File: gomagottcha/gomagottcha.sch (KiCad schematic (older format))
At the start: 77 parts

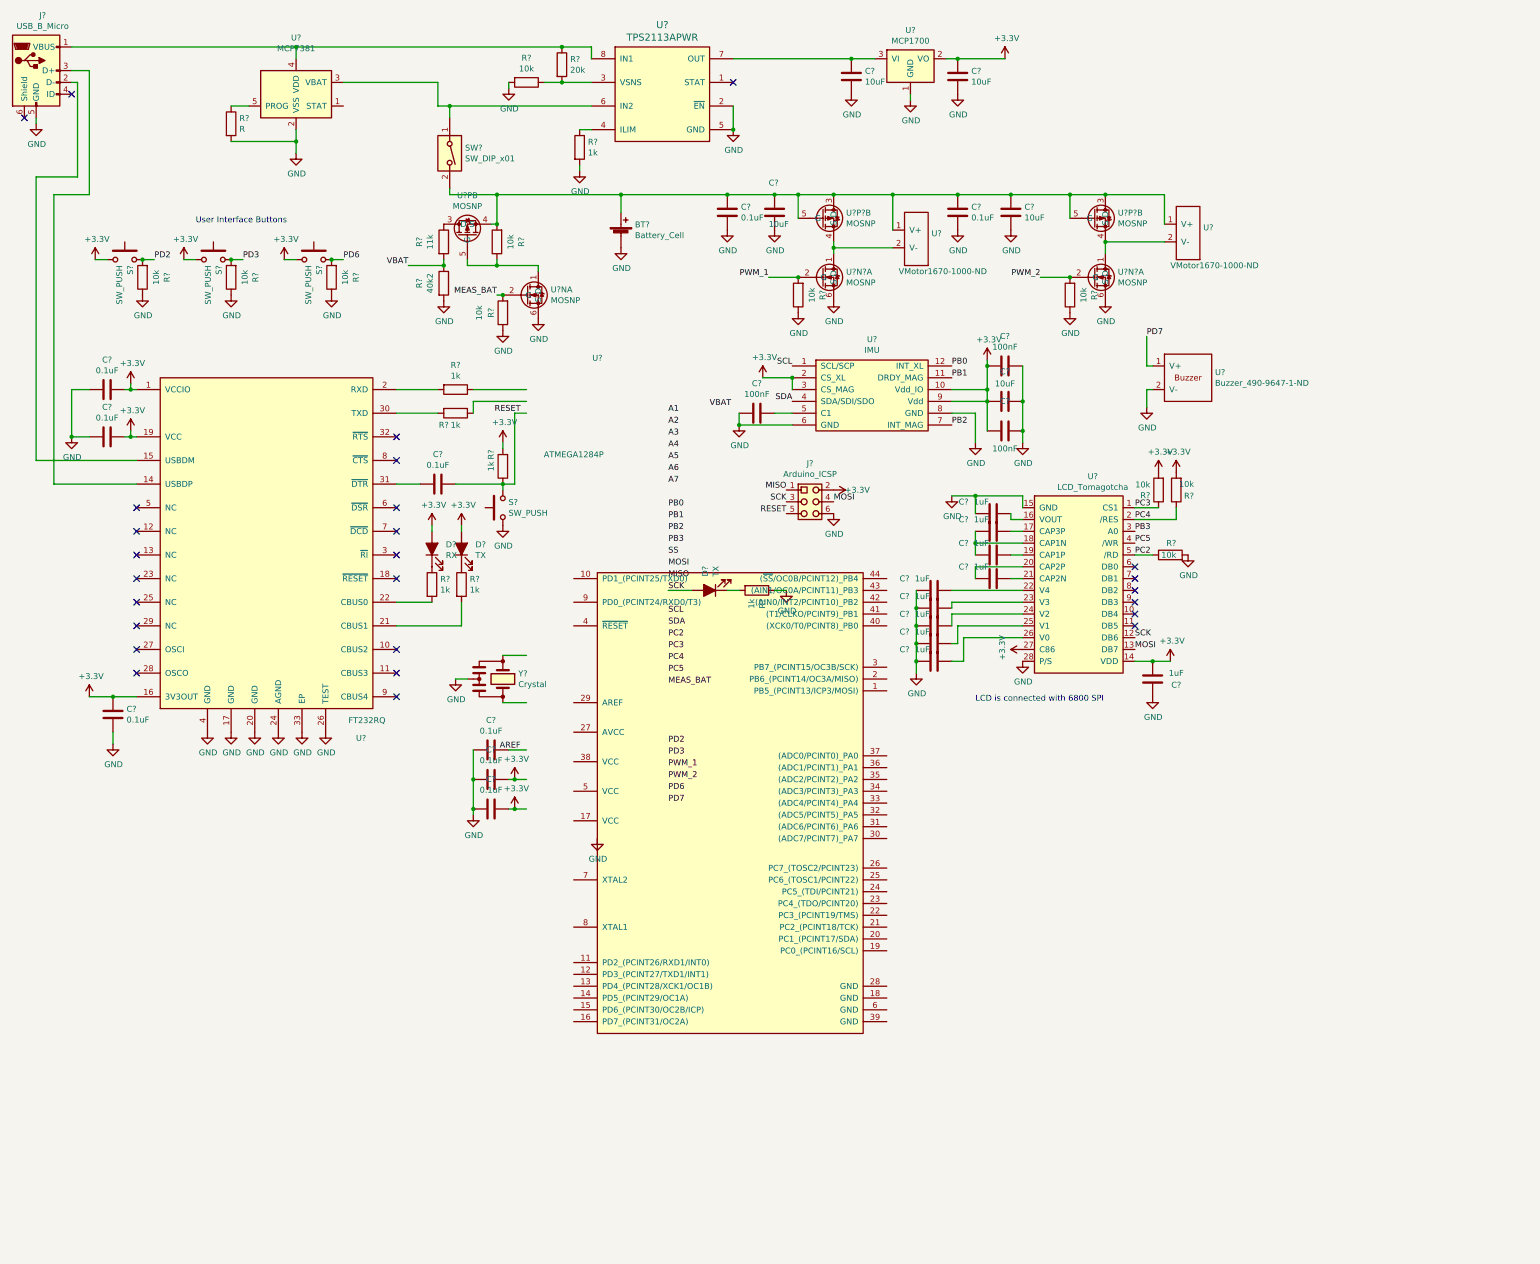
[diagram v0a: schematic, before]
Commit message: BLE hooked up
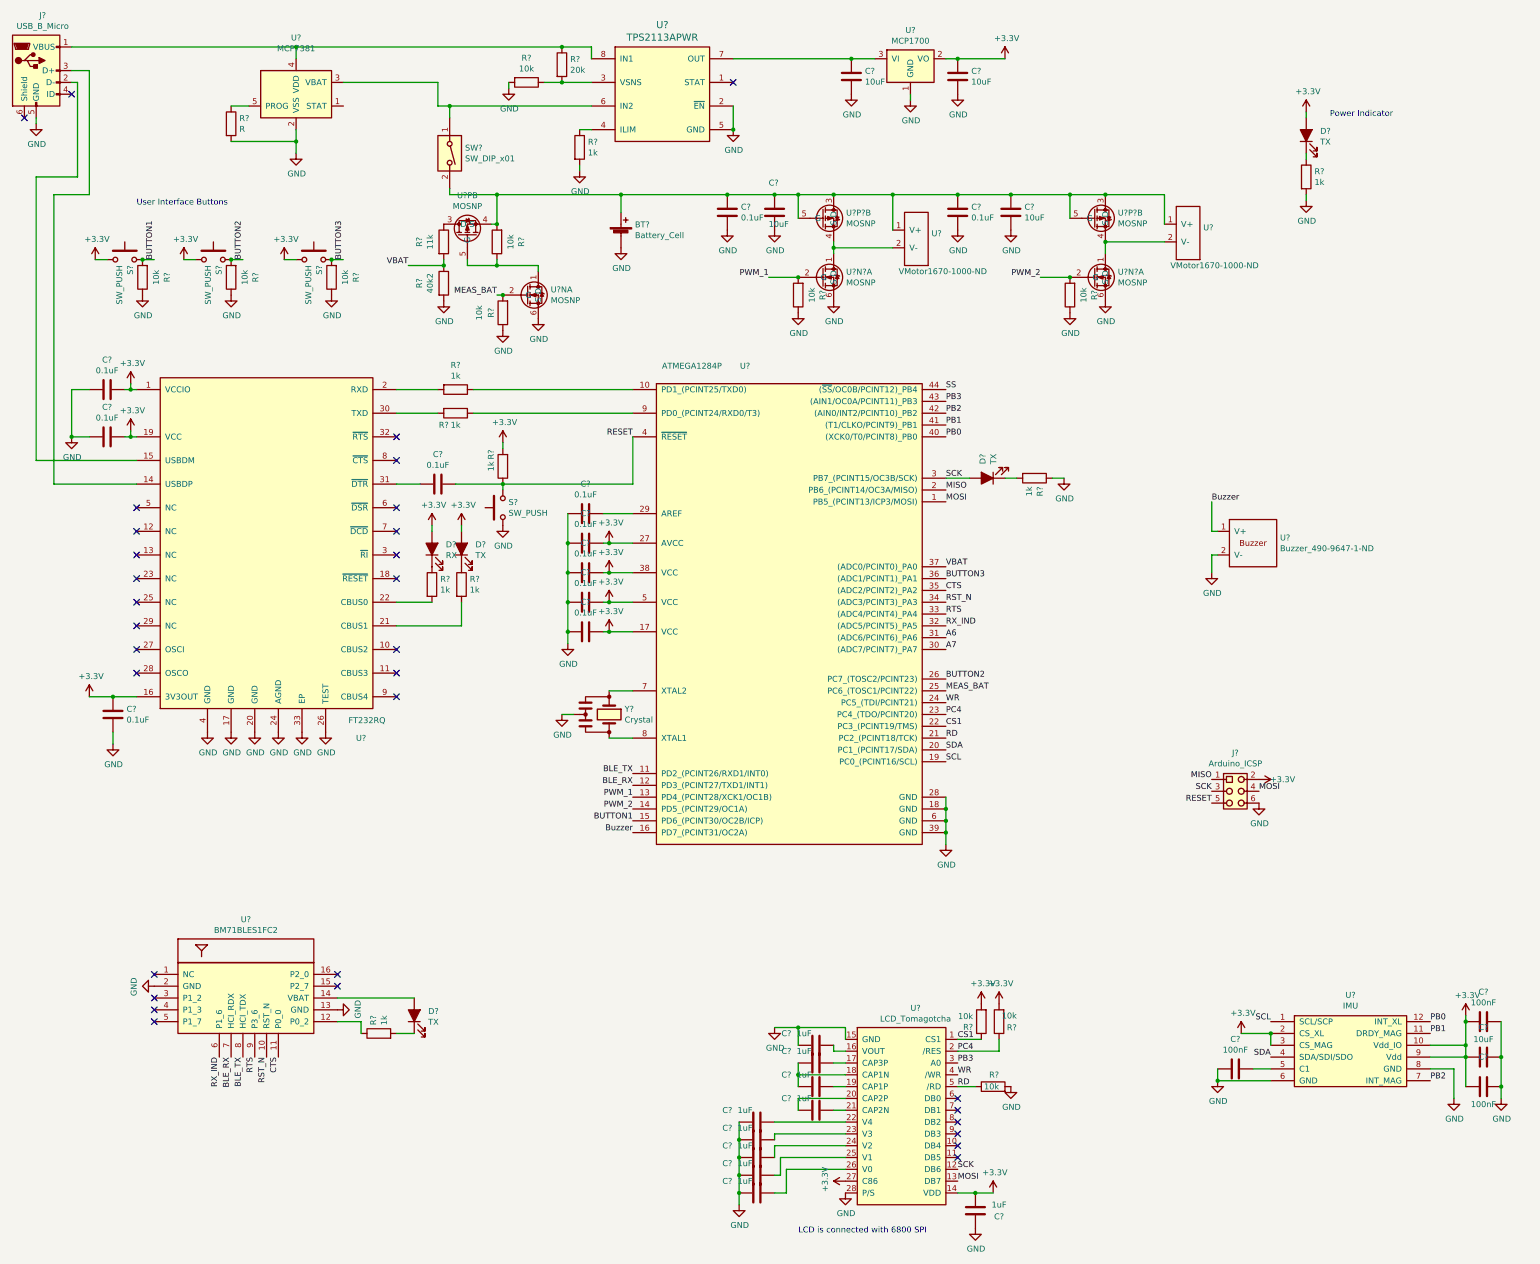
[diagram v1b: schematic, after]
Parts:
- added C? (x2): 0.1uF, symbol tama-sym:C
- added D? (x2): TX, symbol tama-sym:LED_ALT
- added R? (x2): 1k, symbol Device:R
- added U?: BM71BLES1FC2, symbol tama-sym:BM71BLES1FC2
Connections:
- net labels added: BLE_RX, BLE_TX, BUTTON1, BUTTON2, BUTTON3, Buzzer, CS1, CTS, RD, RST_N, RTS, RX_IND, WR
- net labels removed: A1, A2, A3, A4, A5, AREF, PC2, PC3, PC5, PD2, PD3, PD6, PD7
- wire segments 176 -> 191
- no-connect marks 26 -> 32
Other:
- note added: "Power Indicator"
- moved on the sheet: C?, D?, J?, R?, U?, Y?

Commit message: TO DO: Finish assigning footprints
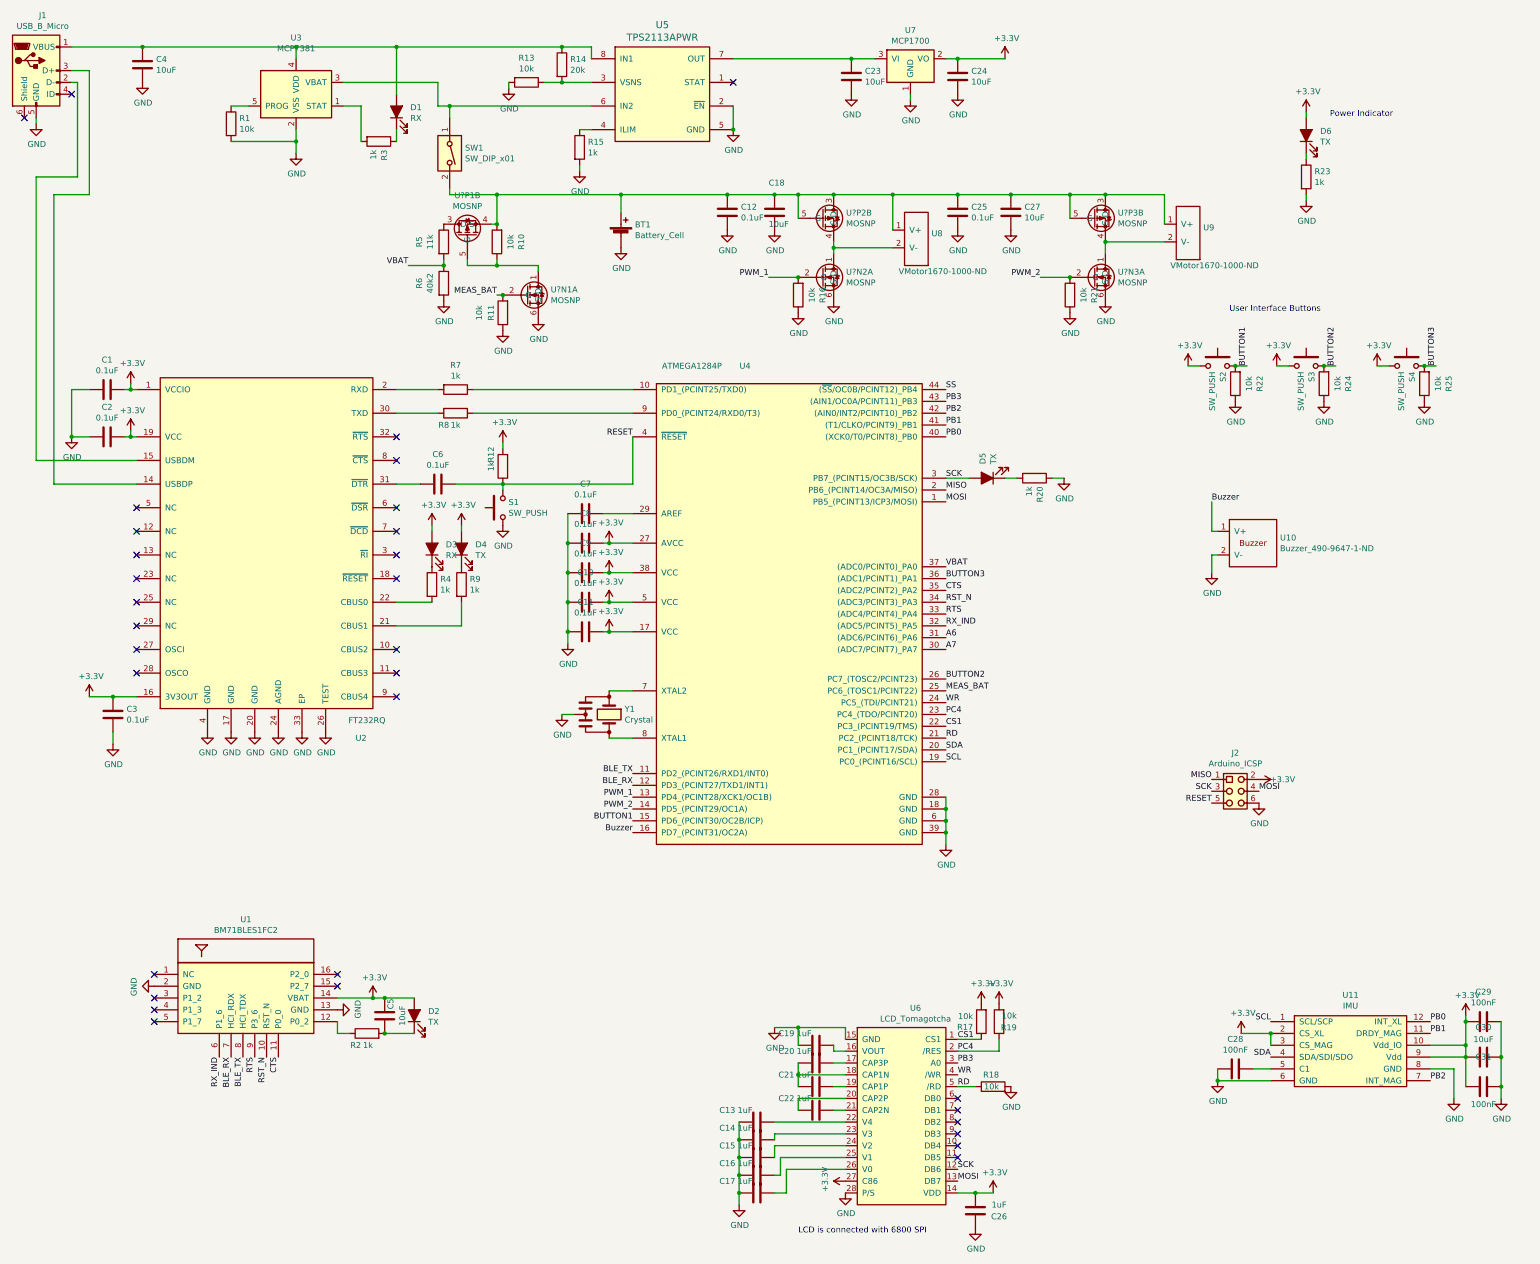
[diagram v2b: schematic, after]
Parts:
- added C4, C5: 10uF, tama-footprints:C_0603_1608Metric, symbol tama-sym:C
- added D1: RX, symbol tama-sym:LED_ALT
- added R3: 1k, tama-footprints:R_0603_1608Metric, symbol Device:R
- C1, C10, C11, C12, C13, C14, C15, C16, C17, C18, C19, C2, C20, C21, C22, C23, C24, C25, C26, C27, C28, C29, C3, C30, C31, C6, C7, C8, C9: renamed from C?; footprint (none) -> tama-footprints:C_0603_1608Metric
- R1: renamed from R?; value R -> 10k; footprint (none) -> tama-footprints:R_0603_1608Metric
- R10, R11, R12, R13, R14, R15, R16, R17, R18, R19, R2, R20, R21, R22, R23, R24, R25, R4, R5, R6, R7, R8, R9: renamed from R?; footprint (none) -> tama-footprints:R_0603_1608Metric
- S1, S2, S3, S4: renamed from S?; footprint (none) -> tama-footprints:Pushbutton_EG4791-ND
- SW1: renamed from SW?; footprint (none) -> tama-footprints:Switch_CWI333-ND
- U1: renamed from U?; footprint (none) -> tama-footprints:BM71BLE
- U2: renamed from U?; footprint Package_SO:TSSOP-28_4.4x9.7mm_P0.65mm -> tama-footprints:QFN-32-1EP_5x5mm_P0.5mm_EP3.1x3.1mm_ThermalVias
- U4: renamed from U?; footprint (none) -> tama-footprints:TQFP-44_10x10mm_P0.8mm
- U5: renamed from U?; footprint Package_SO:TSSOP-8_4.4x3mm_P0.65mm -> tama-footprints:VSON-8_3.1x3.1mm_P0.65mm
- gave numbers to parts that had none: 20
- renumbered U?N to U?N1, U?P to U?P1
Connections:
- net +3V3: now also D2.2 (A), U1.14 (VBAT), C5.1
- net GND: now also C4.2
- net at J1.1 (VBUS), R14.1, U3.4 (VDD)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: now also C4.1, D1.2 (A)
- net at U3.1 (STAT): now also R3.2
- net at D2.1 (K), R2.2: now also C5.2
- new net: D1.1 (K), R3.1
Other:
- moved on the sheet: R2, R22, R24, R25, S2, S3, S4

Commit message: TODO: replace FT232R symbol
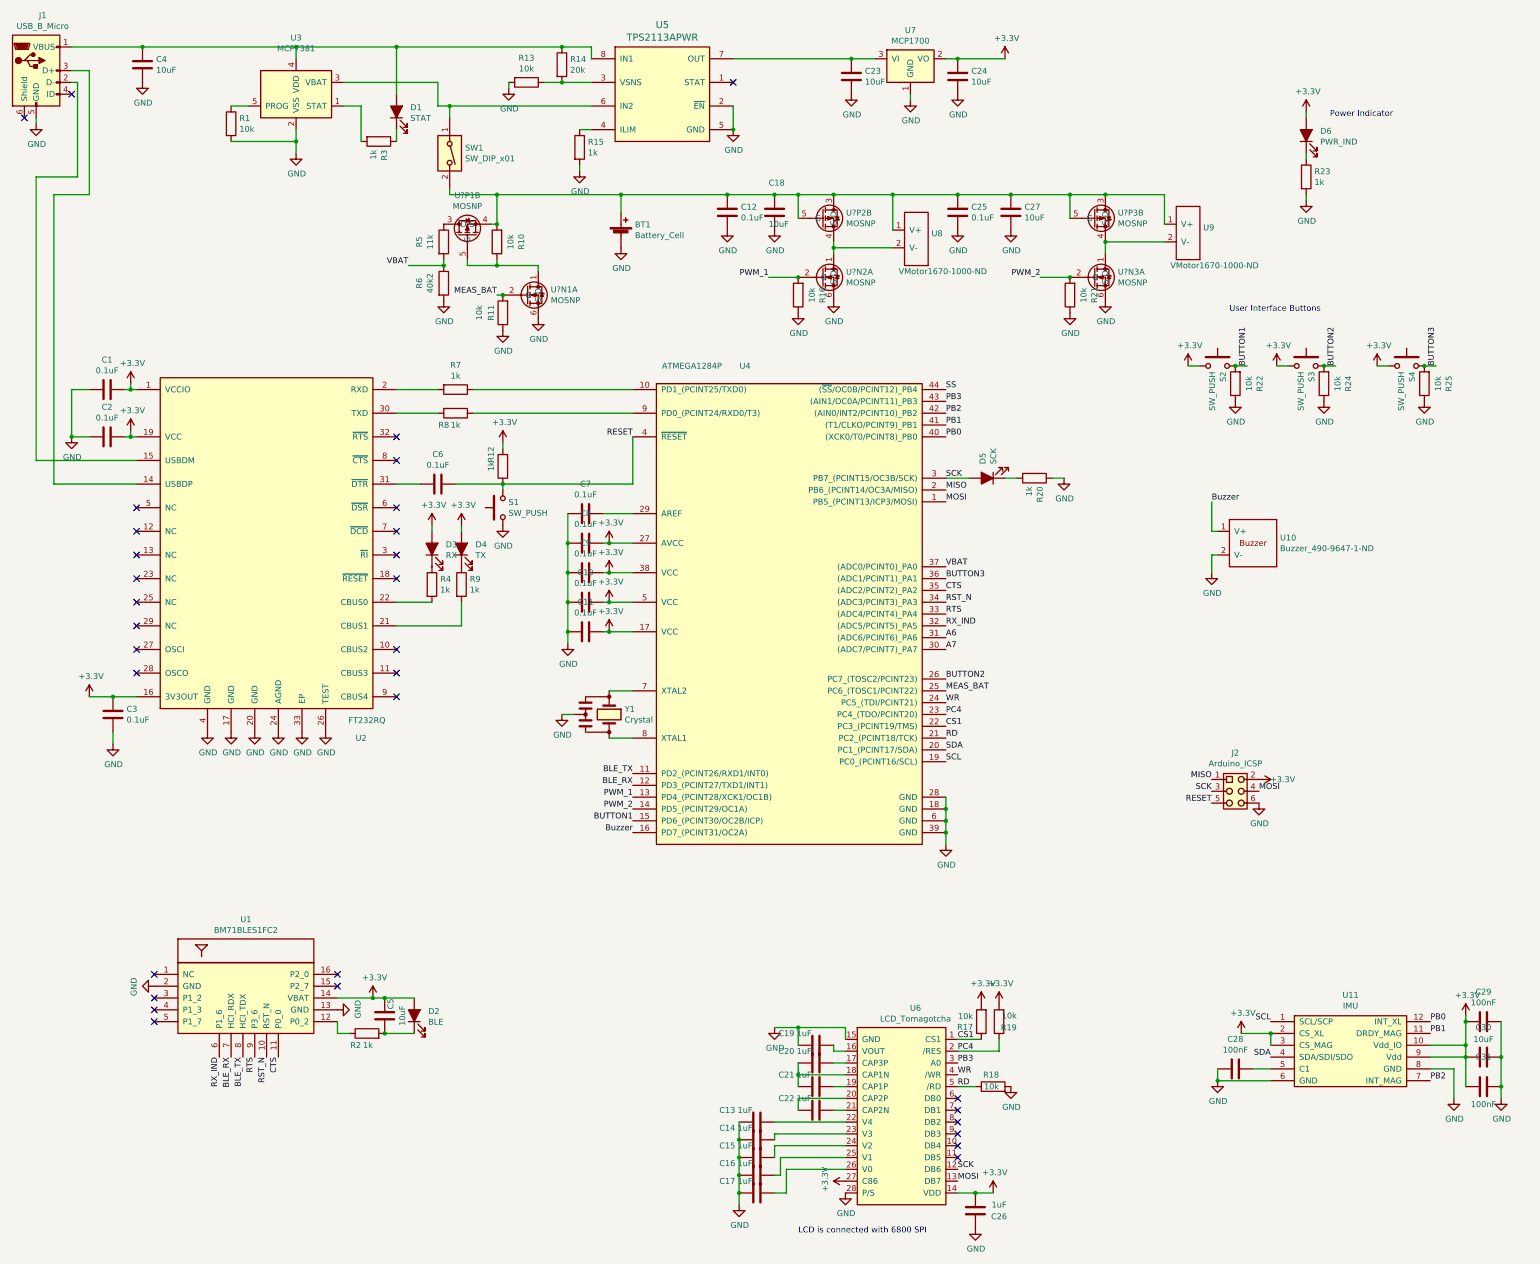
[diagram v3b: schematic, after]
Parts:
- BT1: footprint (none) -> tama-footprints:battery_holder
- D1: value RX -> STAT; footprint (none) -> LED_SMD:LED_0603_1608Metric
- D2: value TX -> BLE; footprint (none) -> LED_SMD:LED_0603_1608Metric
- D3, D4: footprint (none) -> LED_SMD:LED_0603_1608Metric
- D5: value TX -> SCK; footprint (none) -> LED_SMD:LED_0603_1608Metric
- D6: value TX -> PWR_IND; footprint (none) -> LED_SMD:LED_0603_1608Metric
- J2: footprint (none) -> tama-footprints:Arduino_ICSP
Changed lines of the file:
@@
 F 0 "D3" V 4188 4933 50  0000 R CNN
 F 1 "RX" V 4097 4933 50  0000 R CNN
-F 2 "" H 4150 5050 50  0001 C CNN
+F 2 "LED_SMD:LED_0603_1608Metric" H 4150 5050 50  0001 C CNN
 F 3 "~" H 4150 5050 50  0001 C CNN
 	1    4150 5050
@@
 F 0 "D4" V 4438 4932 50  0000 R CNN
 F 1 "TX" V 4347 4932 50  0000 R CNN
-F 2 "" H 4400 5050 50  0001 C CNN
+F 2 "LED_SMD:LED_0603_1608Metric" H 4400 5050 50  0001 C CNN
 F 3 "~" H 4400 5050 50  0001 C CNN
 	1    4400 5050
@@
 P 8850 4450
 F 0 "D5" V 8888 4332 50  0000 R CNN
-F 1 "TX" V 8797 4332 50  0000 R CNN
-F 2 "" H 8850 4450 50  0001 C CNN
+F 1 "SCK" V 8797 4332 50  0000 R CNN
+F 2 "LED_SMD:LED_0603_1608Metric" H 8850 4450 50  0001 C CNN
 F 3 "~" H 8850 4450 50  0001 C CNN
 	1    8850 4450
@@
 F 0 "J2" H 10950 7425 50  0000 C CNN
 F 1 "Arduino_ICSP" H 10950 7334 50  0000 C CNN
-F 2 "" H 10950 7200 50  0001 C CNN
+F 2 "tama-footprints:Arduino_ICSP" H 10950 7200 50  0001 C CNN
 F 3 "" H 10950 7200 50  0001 C CNN
 	1    10950 7100
@@
 F 0 "BT1" H 5868 2496 50  0000 L CNN
 F 1 "Battery_Cell" H 5868 2405 50  0000 L CNN
-F 2 "" V 5750 2460 50  0001 C CNN
+F 2 "tama-footprints:battery_holder" V 5750 2460 50  0001 C CNN
 F 3 "~" V 5750 2460 50  0001 C CNN
 	1    5750 2400
@@
 P 4000 9000
 F 0 "D2" V 4038 8882 50  0000 R CNN
-F 1 "TX" V 3947 8882 50  0000 R CNN
-F 2 "" H 4000 9000 50  0001 C CNN
+F 1 "BLE" V 3947 8882 50  0000 R CNN
+F 2 "LED_SMD:LED_0603_1608Metric" H 4000 9000 50  0001 C CNN
 F 3 "~" H 4000 9000 50  0001 C CNN
 	1    4000 9000
@@
 P 11550 1550
 F 0 "D6" V 11588 1432 50  0000 R CNN
-F 1 "TX" V 11497 1432 50  0000 R CNN
-F 2 "" H 11550 1550 50  0001 C CNN
+F 1 "PWR_IND" V 11497 1432 50  0000 R CNN
+F 2 "LED_SMD:LED_0603_1608Metric" H 11550 1550 50  0001 C CNN
 F 3 "~" H 11550 1550 50  0001 C CNN
 	1    11550 1550
@@
 P 3850 1350
 F 0 "D1" V 3888 1233 50  0000 R CNN
-F 1 "RX" V 3797 1233 50  0000 R CNN
-F 2 "" H 3850 1350 50  0001 C CNN
+F 1 "STAT" V 3797 1233 50  0000 R CNN
+F 2 "LED_SMD:LED_0603_1608Metric" H 3850 1350 50  0001 C CNN
 F 3 "~" H 3850 1350 50  0001 C CNN
 	1    3850 1350
